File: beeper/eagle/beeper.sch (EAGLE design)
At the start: 30 parts, among them J4 ICSP, T1 MMBT3904, U1 ATA6631, U2 ATMEGA328P, X1 16MHz

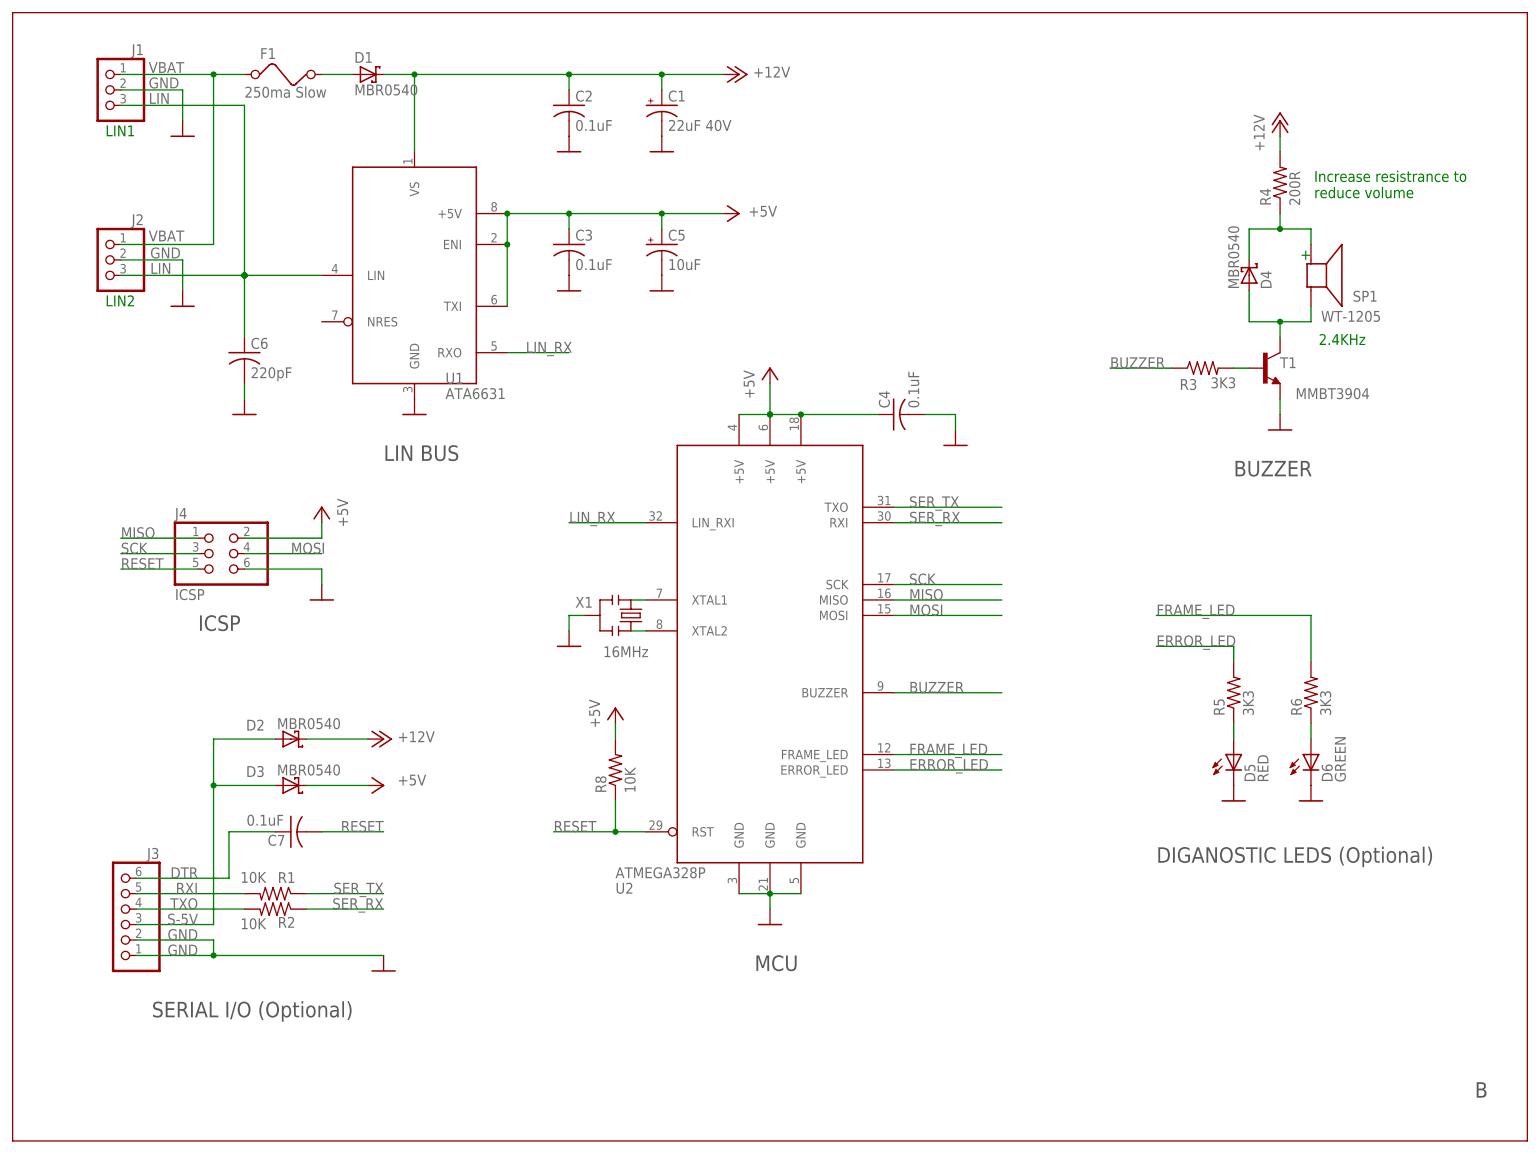
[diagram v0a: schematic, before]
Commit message: Changed the beeper schematic to use the full atmega328p symbol. No Semantic change.
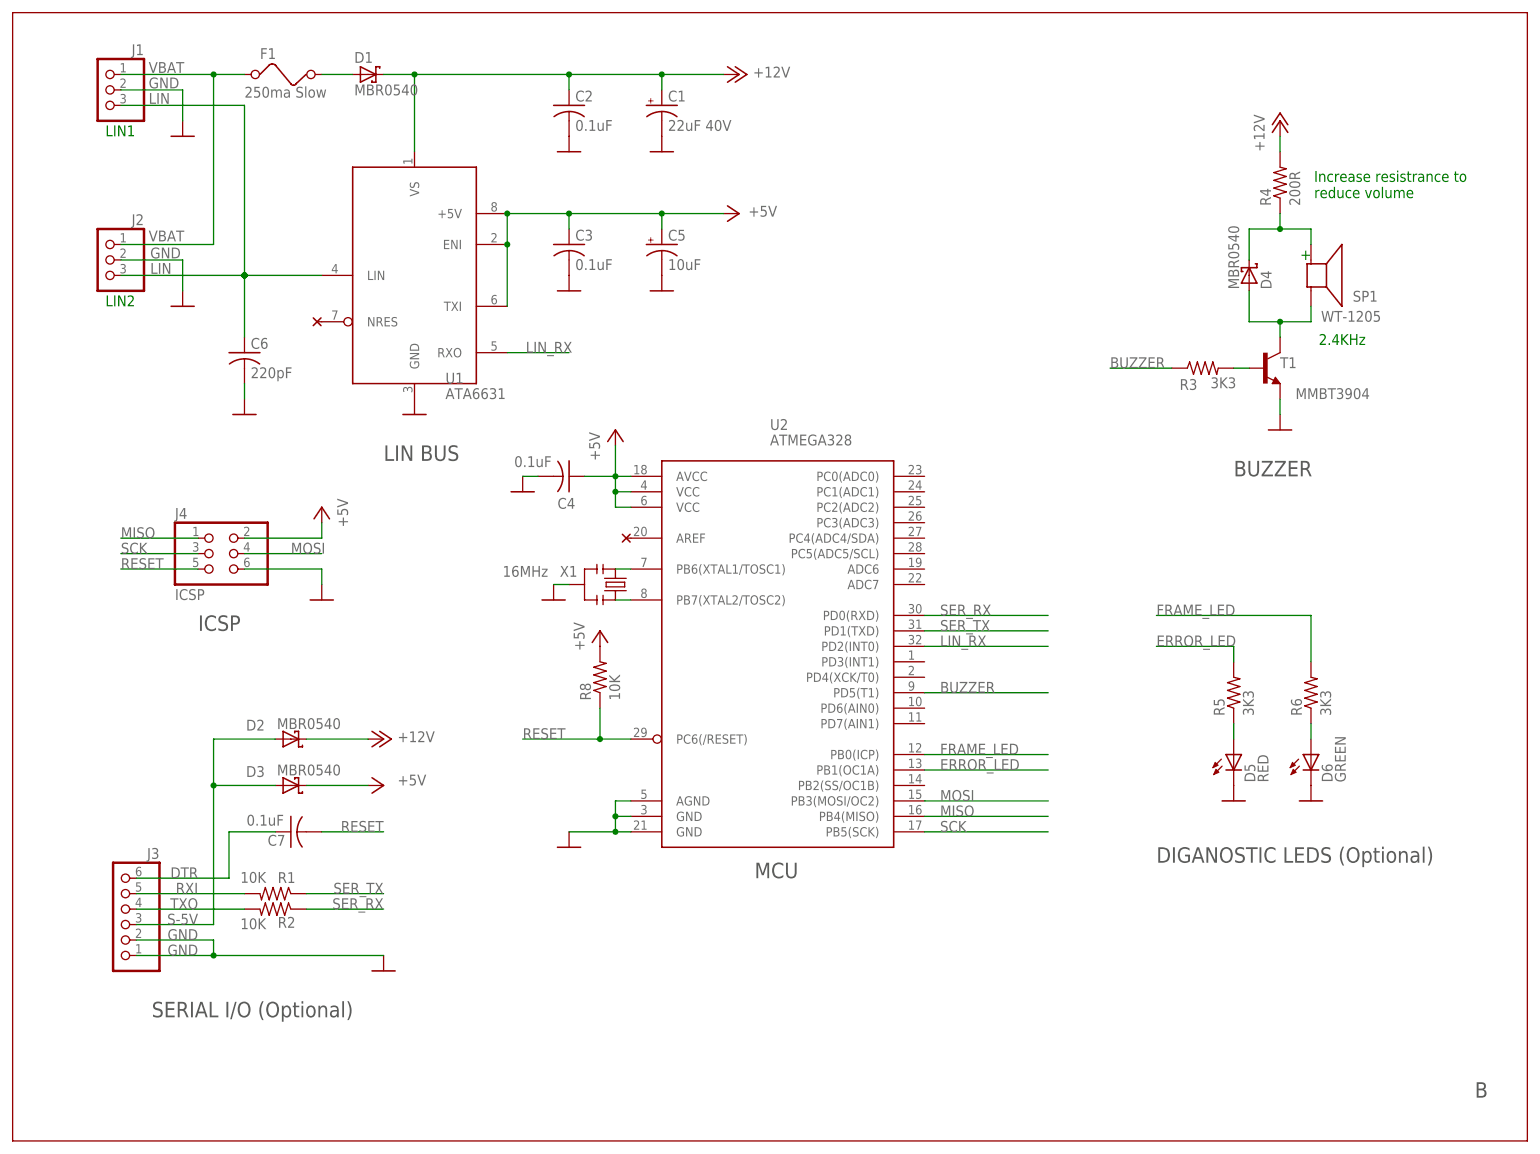
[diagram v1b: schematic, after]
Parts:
- U2: value ATMEGA328P -> ATMEGA328; device beeper:ATMEGA328P -> beeper:ATMEGA328
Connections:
- net +5V: now also U2.AVCC, U2.VCC@1, U2.VCC@2; no longer U2.+5V@1, U2.+5V@2, U2.+5V@3
- net BUZZER: now also U2.PD5(T1); no longer U2.BUZZER
- net ERROR_LED: now also U2.PB1(OC1A); no longer U2.ERROR_LED
- net FRAME_LED: now also U2.PB0(ICP); no longer U2.FRAME_LED
- net GND: now also U2.AGND; no longer U2.GND@3
- net LIN_RX: now also U2.PD2(INT0); no longer U2.LIN_RXI
- net MISO: now also U2.PB4(MISO); no longer U2.MISO
- net MOSI: now also U2.PB3(MOSI/OC2); no longer U2.MOSI
- net RESET: now also U2.PC6(/RESET); no longer U2.RST
- net SCK: now also U2.PB5(SCK); no longer U2.SCK
- net SER_RX: now also U2.PD0(RXD); no longer U2.RXI
- net SER_TX: now also U2.PD1(TXD); no longer U2.TXO
- net XTAL1: now also U2.PB6(XTAL1/TOSC1); no longer U2.XTAL1
- net XTAL2: now also U2.PB7(XTAL2/TOSC2); no longer U2.XTAL2
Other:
- moved on the sheet: C4, R8, X1

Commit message: Completed the beeper schema cleanup. Added NC and debug signal ndicators.
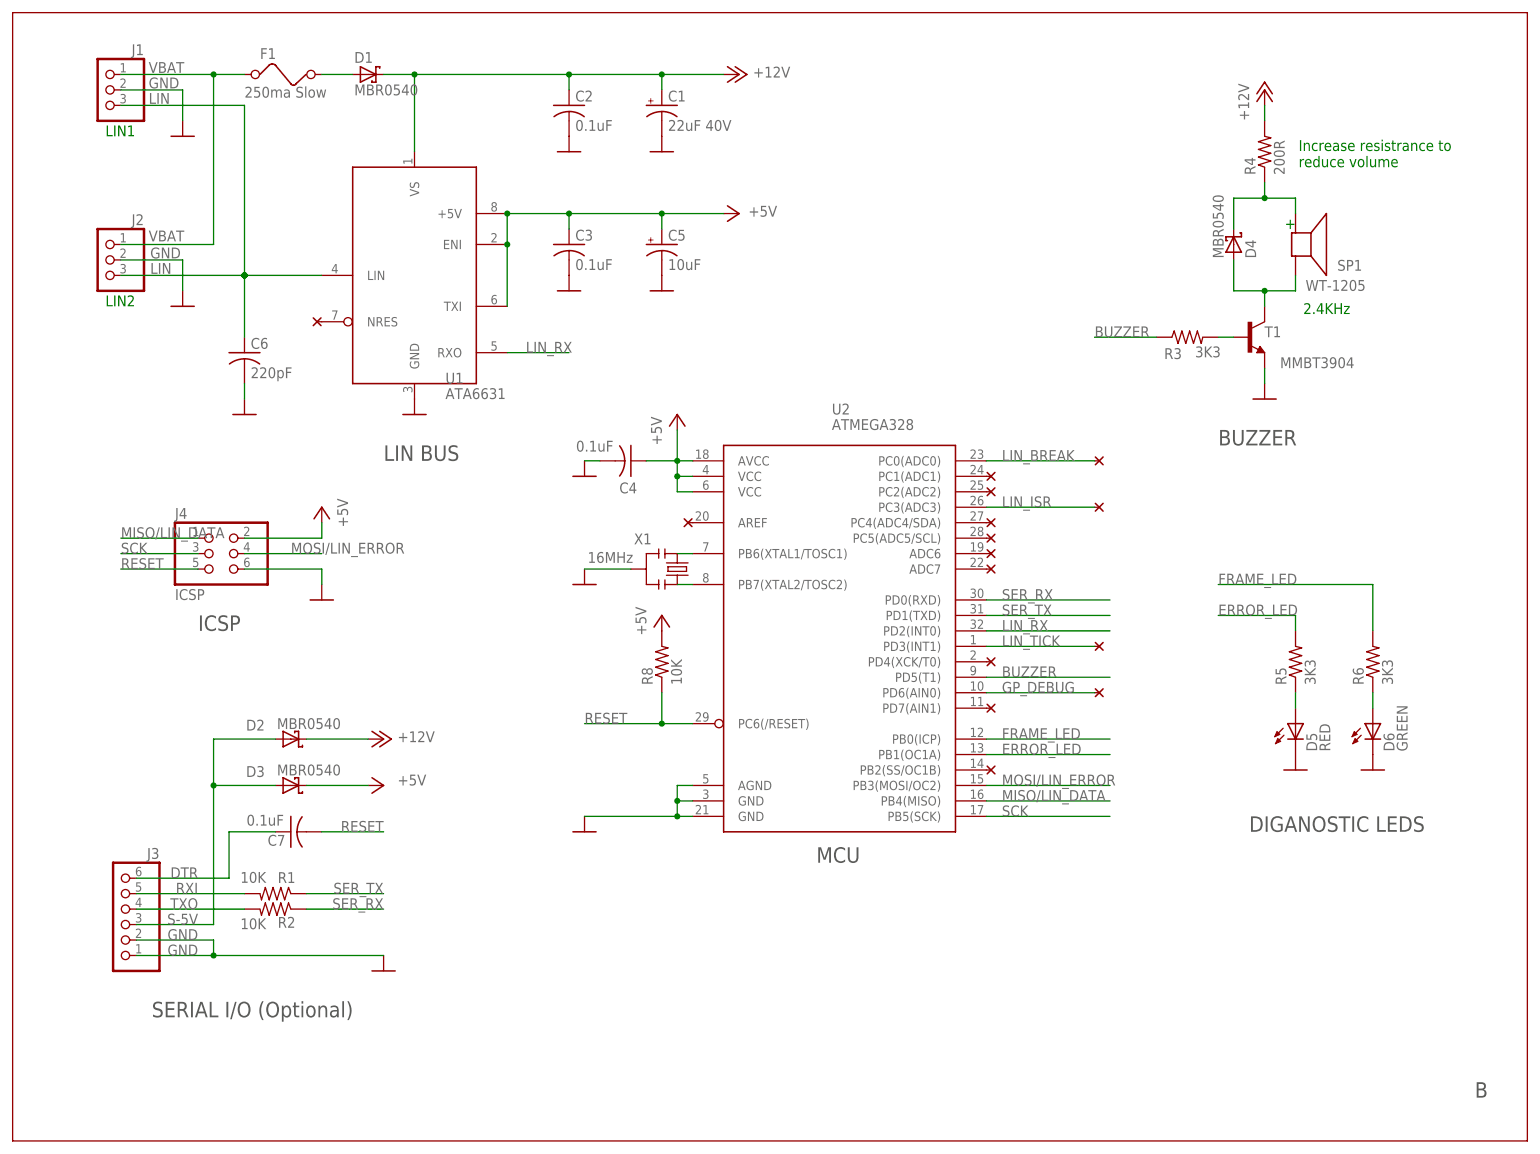
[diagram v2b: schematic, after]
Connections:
- net MISO renamed MISO/LIN_DATA
- net MOSI renamed MOSI/LIN_ERROR
- new net GP_DEBUG: U2.PD6(AIN0)
- new net LIN_BREAK: U2.PC0(ADC0)
- new net LIN_ISR: U2.PC3(ADC3)
- new net LIN_TICK: U2.PD3(INT1)
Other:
- note added: "DIGANOSTIC LEDS"
- note removed: "DIGANOSTIC LEDS (Optional)"
- moved on the sheet: C4, D4, D5, D6, R3, R4, R5, R6, R8, SP1, T1, U2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

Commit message: Minor cosmetic schema changes + TODO list udpate.
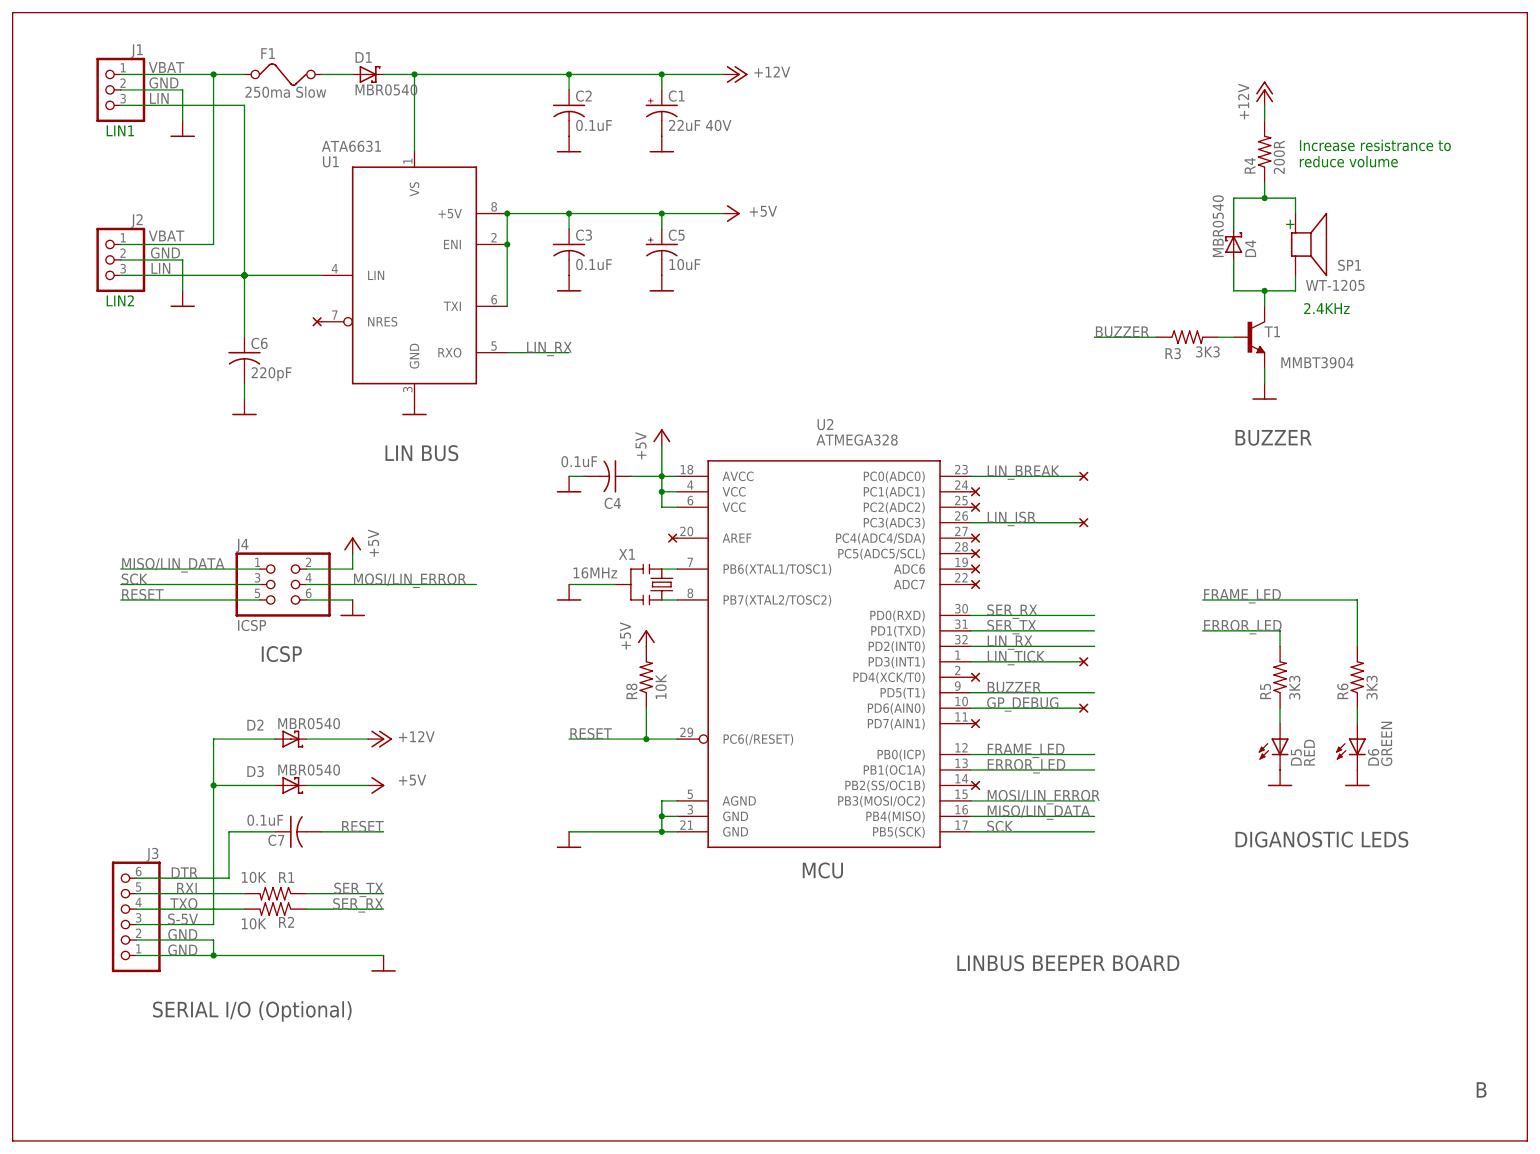
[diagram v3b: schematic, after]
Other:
- note added: "LINBUS BEEPER BOARD"
- moved on the sheet: C4, D5, D6, J4, R5, R6, R8, U2, X1
